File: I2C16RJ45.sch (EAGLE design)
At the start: 86 parts, among them IC1 MCP23017SO, IC2 MCP23017SO, IC3 MCP23017SO, IC4 MCP23017SO, J1 RJ45-X8, J2 RJ45-X8, J3 M06-SOCKET

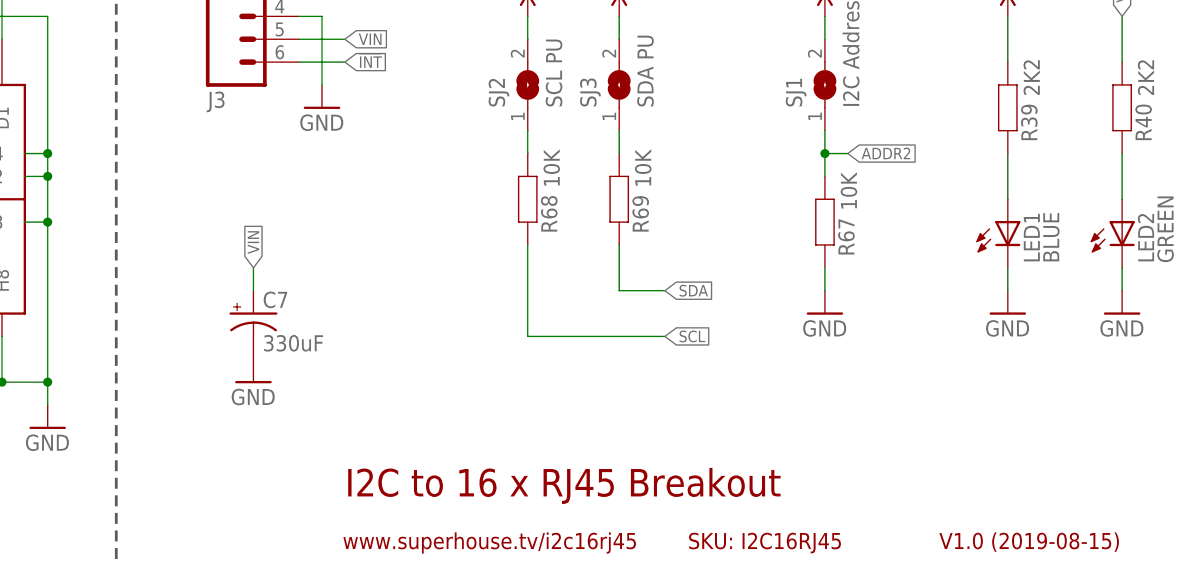
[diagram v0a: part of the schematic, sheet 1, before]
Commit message: Board and schematic labelling
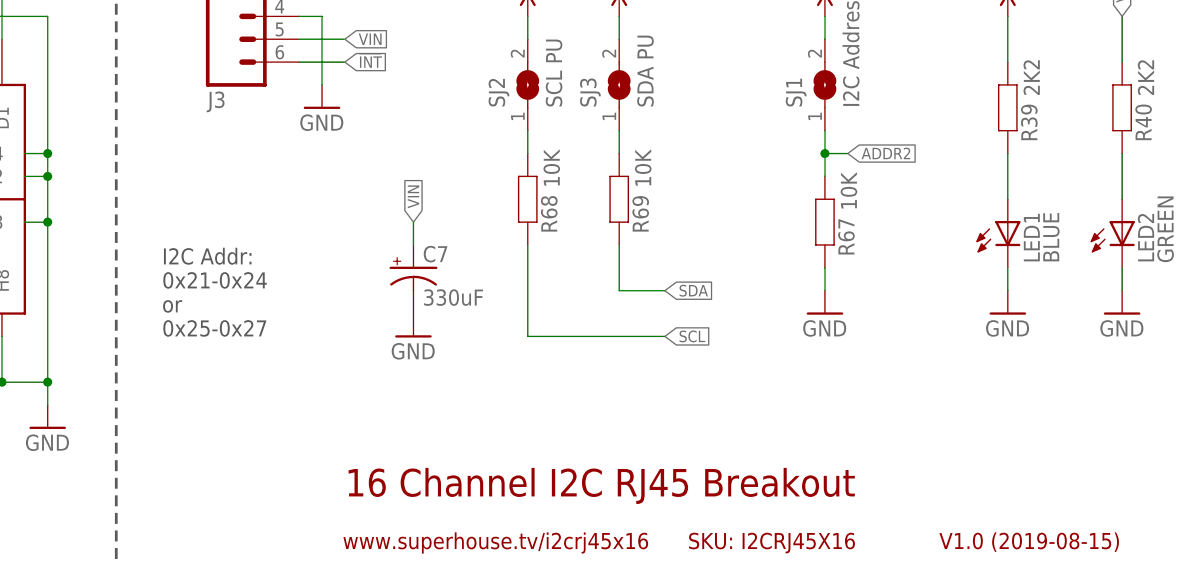
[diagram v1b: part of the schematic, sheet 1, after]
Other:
- note added: "16 Channel I2C RJ45 Breakout"
- note added: "I2C Addr: 0x21-0x24 or 0x25-0x27"
- note added: "SKU: I2CRJ45X16"
- note added: "www.superhouse.tv/i2crj45x16"
- note removed: "I2C to 16 x RJ45 Breakout"
- note removed: "SKU: I2C16RJ45"
- note removed: "www.superhouse.tv/i2c16rj45"
- moved on the sheet: C7
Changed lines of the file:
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@@
 <?xml version="1.0" encoding="utf-8"?>
 <!DOCTYPE eagle SYSTEM "eagle.dtd">
-<eagle version="9.4.2">
+<eagle version="9.5.0">
 <drawing>
 <settings>
@@
 8: GND</text>
 <frame x1="0" y1="0" x2="248.92" y2="185.42" columns="8" rows="5" layer="94"/>
-<text x="149.86" y="12.7" size="3.048" layer="94">I2C to 16 x RJ45 Breakout</text>
+<text x="149.86" y="12.7" size="3.048" layer="94">16 Channel I2C RJ45 Breakout</text>
 <text x="215.9" y="6.858" size="1.778" layer="94">V1.0 (2019-08-15)</text>
-<text x="149.606" y="6.858" size="1.778" layer="94">www.superhouse.tv/i2c16rj45</text>
-<text x="187.96" y="6.858" size="1.778" layer="94">SKU: I2C16RJ45</text>
+<text x="149.606" y="6.858" size="1.778" layer="94">www.superhouse.tv/i2crj45x16</text>
+<text x="187.96" y="6.858" size="1.778" layer="94">SKU: I2CRJ45X16</text>
 <frame x1="147.32" y1="5.08" x2="243.84" y2="17.78" columns="0" rows="0" layer="94" border-left="no" border-top="no" border-right="no" border-bottom="no"/>
 <frame x1="185.42" y1="5.08" x2="213.36" y2="10.16" columns="8" rows="5" layer="94"/>
@@
 <text x="12.7" y="99.06" size="1.778" layer="97">I2C Addr: 0x20/0x24</text>
 <text x="132.08" y="99.06" size="1.778" layer="97">I2C Addr: 0x21/0x25</text>
+<text x="129.54" y="30.48" size="1.778" layer="97">I2C Addr:
+0x21-0x24
+or
+0x25-0x27</text>
 </plain>
 <instances>
@@
 <attribute name="VALUE" x="182.118" y="46.99" size="1.778" layer="96" rot="MR90"/>
 </instance>
-<instance part="C7" gate="G$1" x="139.7" y="33.02" smashed="yes">
-<attribute name="NAME" x="140.716" y="33.655" size="1.778" layer="95"/>
-<attribute name="VALUE" x="140.716" y="28.829" size="1.778" layer="96"/>
-</instance>
-<instance part="GND11" gate="1" x="139.7" y="25.4" smashed="yes">
-<attribute name="VALUE" x="137.16" y="22.86" size="1.778" layer="96"/>
+<instance part="C7" gate="G$1" x="157.48" y="38.1" smashed="yes">
+<attribute name="NAME" x="158.496" y="38.735" size="1.778" layer="95"/>
+<attribute name="VALUE" x="158.496" y="33.909" size="1.778" layer="96"/>
+</instance>
+<instance part="GND11" gate="1" x="157.48" y="30.48" smashed="yes">
+<attribute name="VALUE" x="154.94" y="27.94" size="1.778" layer="96"/>
 </instance>
 </instances>
@@
 <segment>
 <pinref part="C7" gate="G$1" pin="+"/>
-<wire x1="139.7" y1="35.56" x2="139.7" y2="38.1" width="0.1524" layer="91"/>
-<label x="139.7" y="38.1" size="1.27" layer="95" rot="R90" xref="yes"/>
+<wire x1="157.48" y1="40.64" x2="157.48" y2="43.18" width="0.1524" layer="91"/>
+<label x="157.48" y="43.18" size="1.27" layer="95" rot="R90" xref="yes"/>
 </segment>
 </net>
@@
 <sheet>
 <plain>
-<text x="7.62" y="30.48" size="1.778" layer="97">RJ45 Pins
+<text x="5.08" y="30.48" size="1.778" layer="97">RJ45 Pins
 1: Data 1
 2: Data 2

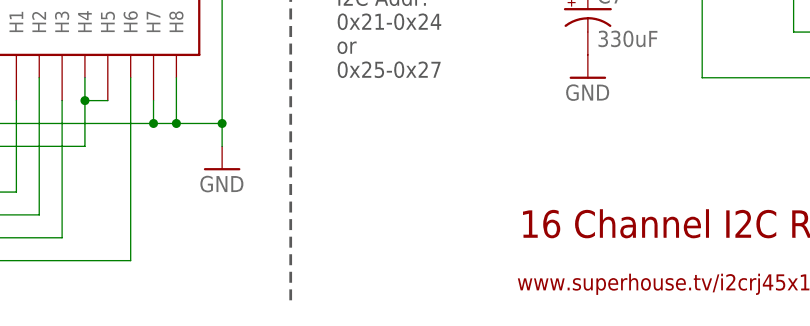
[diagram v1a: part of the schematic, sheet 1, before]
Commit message: Added fiducials
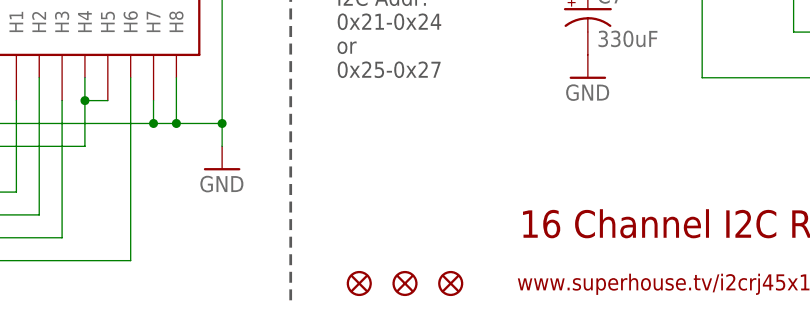
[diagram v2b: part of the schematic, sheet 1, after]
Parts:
- added FID1, FID2, FID3: FIDUCIAL1X2.5, freetronics:FIDUCIAL1X2.5
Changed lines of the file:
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@@
 <part name="C7" library="SuperHouse-DiscreteSemi" library_urn="urn:adsk.eagle:library:11768461" deviceset="CAP_POL" device="G" package3d_urn="urn:adsk.eagle:package:7066306/2" value="330uF"/>
 <part name="GND11" library="SuperHouse-SupplySymbols" library_urn="urn:adsk.eagle:library:11790503" deviceset="GND" device=""/>
+<part name="FID1" library="freetronics" deviceset="FIDUCIAL" device="1X2.5"/>
+<part name="FID2" library="freetronics" deviceset="FIDUCIAL" device="1X2.5"/>
+<part name="FID3" library="freetronics" deviceset="FIDUCIAL" device="1X2.5"/>
 </parts>
 <sheets>
@@
 <attribute name="VALUE" x="154.94" y="27.94" size="1.778" layer="96"/>
 </instance>
+<instance part="FID1" gate="G$1" x="137.16" y="7.62" smashed="yes"/>
+<instance part="FID2" gate="G$1" x="142.24" y="7.62" smashed="yes"/>
+<instance part="FID3" gate="G$1" x="132.08" y="7.62" smashed="yes"/>
 </instances>
 <busses>
